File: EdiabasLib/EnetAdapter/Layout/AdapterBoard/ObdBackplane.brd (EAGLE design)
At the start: 32 x 19.5 mm, 11 parts

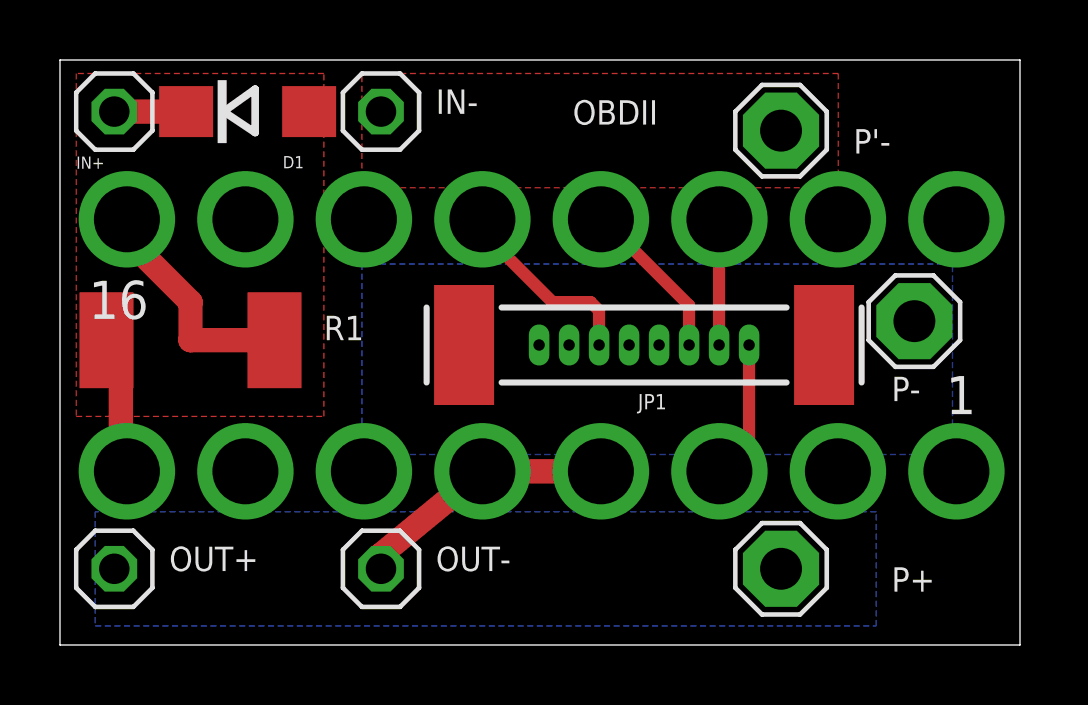
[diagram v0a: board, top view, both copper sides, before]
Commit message: Added second optional hole
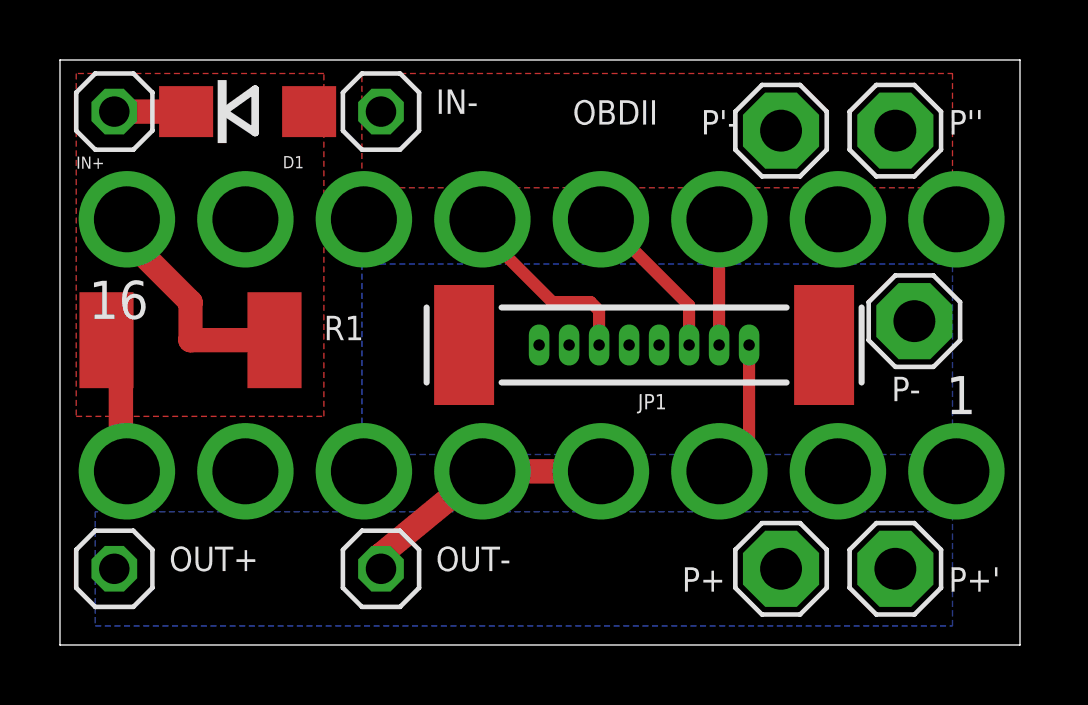
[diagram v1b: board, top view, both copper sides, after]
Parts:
- added P'', P+': SE14, solpad:SE14
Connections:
- net +5V: now also P+'.MP
- net GND2: now also P''.MP
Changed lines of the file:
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@@
 </element>
 <element name="P+" library="solpad" library_urn="urn:adsk.eagle:library:364" package="SE14" package3d_urn="urn:adsk.eagle:package:26504/1" value="SE14" x="26.035" y="2.54" smashed="yes">
-<attribute name="NAME" x="29.718" y="1.778" size="0.8128" layer="25" ratio="10"/>
+<attribute name="NAME" x="22.733" y="1.778" size="0.8128" layer="25" ratio="10"/>
 </element>
 <element name="P-" library="solpad" library_urn="urn:adsk.eagle:library:364" package="SE14" package3d_urn="urn:adsk.eagle:package:26504/1" value="SE14" x="30.48" y="10.795" smashed="yes">
@@
 </element>
 <element name="P'-" library="solpad" library_urn="urn:adsk.eagle:library:364" package="SE14" package3d_urn="urn:adsk.eagle:package:26504/1" value="SE14" x="26.035" y="17.145" smashed="yes">
-<attribute name="NAME" x="28.448" y="16.383" size="0.8128" layer="25" ratio="10"/>
+<attribute name="NAME" x="23.368" y="17.018" size="0.8128" layer="25" ratio="10"/>
+</element>
+<element name="P''" library="solpad" library_urn="urn:adsk.eagle:library:364" package="SE14" package3d_urn="urn:adsk.eagle:package:26504/1" value="SE14" x="29.845" y="17.145" smashed="yes">
+<attribute name="NAME" x="31.623" y="17.018" size="0.8128" layer="25" ratio="10"/>
+<attribute name="VALUE" x="29.845" y="17.526" size="0.0254" layer="27"/>
+</element>
+<element name="P+'" library="solpad" library_urn="urn:adsk.eagle:library:364" package="SE14" package3d_urn="urn:adsk.eagle:package:26504/1" value="SE14" x="29.845" y="2.54" smashed="yes">
+<attribute name="NAME" x="31.623" y="1.778" size="0.8128" layer="25" ratio="10"/>
+<attribute name="VALUE" x="29.845" y="2.921" size="0.0254" layer="27"/>
 </element>
 </elements>
@@
 <polygon width="0.254" layer="16" spacing="0.254" isolate="0.4064">
 <vertex x="3.175" y="0.635"/>
-<vertex x="29.21" y="0.635"/>
-<vertex x="29.21" y="4.445"/>
+<vertex x="31.75" y="0.635"/>
+<vertex x="31.75" y="4.445"/>
 <vertex x="3.175" y="4.445"/>
 </polygon>
 <contactref element="P+" pad="MP"/>
+<contactref element="P+'" pad="MP"/>
 </signal>
 <signal name="N$3">
@@
 <polygon width="0.254" layer="1" spacing="0.254" isolate="0.4064">
 <vertex x="12.065" y="19.05"/>
-<vertex x="27.94" y="19.05"/>
-<vertex x="27.94" y="15.24"/>
+<vertex x="31.75" y="19.05"/>
+<vertex x="31.75" y="15.24"/>
 <vertex x="12.065" y="15.24"/>
 </polygon>
+<contactref element="P''" pad="MP"/>
 </signal>
 </signals>
